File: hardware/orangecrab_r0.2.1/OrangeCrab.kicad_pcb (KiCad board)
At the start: 6 copper layers, 50.8 x 22.9 mm, 163 parts, among them J1 Conn_01x12_Male, J2 Conn_01x16_Male, J3 USB_C_Receptacle_USB2.0, J4 MicroSd, J5 JST, J6 Conn_01x05_Male, SW1 SW_Push, U1 TLV62569DRL, U10 NCP115-2.5, U2 TLV62569DRL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

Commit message: Added revision suffix gc1 to indicate the changed layout: 0.2.1-gc1
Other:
- board text added: "r0.2.1-gc1"
- board text removed: "r0.2.1"
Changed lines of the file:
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@@
 		(title "Orange Crab")
 		(date "2020-07-18")
-		(rev "r0.2.1")
+		(rev "r0.2.1-gc1")
 		(company "Good Stuff Department")
 		(comment 1 "ECP5 in Feather format with DDR3 x16 memory")
@@
 		)
 	)
-	(gr_text "r0.2.1"
+	(gr_text "r0.2.1-gc1"
 		(at 172.57 101.04 0)
 		(layer "B.SilkS")

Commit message: 0.2.1-gc2: Centered castelated holes to edges and reduced diameter from 1 to 0.8 mm
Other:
- board text added: "r0.2.1-gc2"
- board text removed: "r0.2.1-gc1"
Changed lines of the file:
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@@
 	(title_block
 		(title "Orange Crab")
-		(date "2020-07-18")
-		(rev "r0.2.1-gc1")
+		(date "2026-01-30")
+		(rev "r0.2.1-gc2")
 		(company "Good Stuff Department")
 		(comment 1 "ECP5 in Feather format with DDR3 x16 memory")
 		(comment 3 "Licensed under CERN OHL v.1.2")
-		(comment 4 "Designed By: Gregory Davill")
+		(comment 4 "Originally Designed By: Gregory Davill")
 	)
 	(layers
@@
 		)
 		(pad "1" thru_hole roundrect
-			(at -13.97 -1.4)
+			(at -13.97 -1.27)
 			(size 2 2)
-			(drill 1)
+			(drill 0.8)
 			(layers "*.Cu" "*.Mask")
 			(remove_unused_layers no)
@@
 		)
 		(pad "2" thru_hole circle
-			(at -11.43 -1.4)
+			(at -11.43 -1.27)
 			(size 2 2)
-			(drill 1)
+			(drill 0.8)
 			(layers "*.Cu" "*.Mask")
 			(remove_unused_layers no)
@@
 		)
 		(pad "3" thru_hole circle
-			(at -8.89 -1.4)
+			(at -8.89 -1.27)
 			(size 2 2)
-			(drill 1)
+			(drill 0.8)
 			(layers "*.Cu" "*.Mask")
 			(remove_unused_layers no)
@@
 		)
 		(pad "4" thru_hole circle
-			(at -6.35 -1.4)
+			(at -6.35 -1.27)
 			(size 2 2)
-			(drill 1)
+			(drill 0.8)
 			(layers "*.Cu" "*.Mask")
 			(remove_unused_layers no)
@@
 		)
 		(pad "5" thru_hole circle
-			(at -3.81 -1.4)
+			(at -3.81 -1.27)
 			(size 2 2)
-			(drill 1)
+			(drill 0.8)
 			(layers "*.Cu" "*.Mask")
 			(remove_unused_layers no)
@@
 		)
 		(pad "6" thru_hole circle
-			(at -1.27 -1.4)
+			(at -1.27 -1.27)
 			(size 2 2)
-			(drill 1)
+			(drill 0.8)
 			(layers "*.Cu" "*.Mask")
 			(remove_unused_layers no)
@@
 		)
 		(pad "7" thru_hole circle
-			(at 1.27 -1.4)
+			(at 1.27 -1.27)
 			(size 2 2)
-			(drill 1)
+			(drill 0.8)
 			(layers "*.Cu" "*.Mask")
 			(remove_unused_layers no)
@@
 		)
 		(pad "8" thru_hole circle
-			(at 3.81 -1.4)
+			(at 3.81 -1.27)
 			(size 2 2)
-			(drill 1)
+			(drill 0.8)
 			(layers "*.Cu" "*.Mask")
 			(remove_unused_layers no)
@@
 		)
 		(pad "9" thru_hole circle
-			(at 6.35 -1.4)
+			(at 6.35 -1.27)
 			(size 2 2)
-			(drill 1)
+			(drill 0.8)
 			(layers "*.Cu" "*.Mask")
 			(remove_unused_layers no)
@@
 		)
 		(pad "10" thru_hole circle
-			(at 8.89 -1.4)
+			(at 8.89 -1.27)
 			(size 2 2)
-			(drill 1)
+			(drill 0.8)
 			(layers "*.Cu" "*.Mask")
 			(remove_unused_layers no)
@@
 		)
 		(pad "11" thru_hole circle
-			(at 11.43 -1.4)
+			(at 11.43 -1.27)
 			(size 2 2)
-			(drill 1)
+			(drill 0.8)
 			(layers "*.Cu" "*.Mask")
 			(remove_unused_layers no)
@@
 		)
 		(pad "12" thru_hole circle
-			(at 13.97 -1.4)
+			(at 13.97 -1.27)
 			(size 2 2)
-			(drill 1)
+			(drill 0.8)
 			(layers "*.Cu" "*.Mask")
 			(remove_unused_layers no)
@@
 		)
 		(pad "1" thru_hole roundrect
-			(at -19.05 1.4)
+			(at -19.05 1.27)
 			(size 2 2)
-			(drill 1)
+			(drill 0.8)
 			(layers "*.Cu" "*.Mask")
 			(remove_unused_layers no)
@@
 		)
 		(pad "2" thru_hole circle
-			(at -16.51 1.4)
+			(at -16.51 1.27)
 			(size 2 2)
-			(drill 1)
+			(drill 0.8)
 			(layers "*.Cu" "*.Mask")
 			(remove_unused_layers no)
@@
 		)
 		(pad "3" thru_hole circle
-			(at -13.97 1.4)
+			(at -13.97 1.27)
 			(size 2 2)
-			(drill 1)
+			(drill 0.8)
 			(layers "*.Cu" "*.Mask")
 			(remove_unused_layers no)
@@
 		)
 		(pad "4" thru_hole circle
-			(at -11.43 1.4)
+			(at -11.43 1.27)
 			(size 2 2)
-			(drill 1)
+			(drill 0.8)
 			(layers "*.Cu" "*.Mask")
 			(remove_unused_layers no)
@@
 		)
 		(pad "5" thru_hole circle
-			(at -8.89 1.4)
+			(at -8.89 1.27)
 			(size 2 2)
-			(drill 1)
+			(drill 0.8)
 			(layers "*.Cu" "*.Mask")
 			(remove_unused_layers no)
@@
 		)
 		(pad "6" thru_hole circle
-			(at -6.35 1.4)
+			(at -6.35 1.27)
 			(size 2 2)
-			(drill 1)
+			(drill 0.8)
 			(layers "*.Cu" "*.Mask")
 			(remove_unused_layers no)
@@
 		)
 		(pad "7" thru_hole circle
-			(at -3.81 1.4)
+			(at -3.81 1.27)
 			(size 2 2)
-			(drill 1)
+			(drill 0.8)
 			(layers "*.Cu" "*.Mask")
 			(remove_unused_layers no)
@@
 		)
 		(pad "8" thru_hole circle
-			(at -1.27 1.4)
+			(at -1.27 1.27)
 			(size 2 2)
-			(drill 1)
+			(drill 0.8)
 			(layers "*.Cu" "*.Mask")
 			(remove_unused_layers no)
@@
 		)
 		(pad "9" thru_hole circle
-			(at 1.27 1.4)
+			(at 1.27 1.27)
 			(size 2 2)
-			(drill 1)
+			(drill 0.8)
 			(layers "*.Cu" "*.Mask")
 			(remove_unused_layers no)
@@
 		)
 		(pad "10" thru_hole circle
-			(at 3.81 1.4)
+			(at 3.81 1.27)
 			(size 2 2)
-			(drill 1)
+			(drill 0.8)
 			(layers "*.Cu" "*.Mask")
 			(remove_unused_layers no)
@@
 		)
 		(pad "11" thru_hole circle
-			(at 6.35 1.4)
+			(at 6.35 1.27)
 			(size 2 2)
-			(drill 1)
+			(drill 0.8)
 			(layers "*.Cu" "*.Mask")
 			(remove_unused_layers no)
@@
 		)
 		(pad "12" thru_hole circle
-			(at 8.89 1.4)
+			(at 8.89 1.27)
 			(size 2 2)
-			(drill 1)
+			(drill 0.8)
 			(layers "*.Cu" "*.Mask")
 			(remove_unused_layers no)
@@
 		)
 		(pad "13" thru_hole circle
-			(at 11.43 1.4)
+			(at 11.43 1.27)
 			(size 2 2)
-			(drill 1)
+			(drill 0.8)
 			(layers "*.Cu" "*.Mask")
 			(remove_unused_layers no)
@@
 		)
 		(pad "14" thru_hole circle
-			(at 13.97 1.4)
+			(at 13.97 1.27)
 			(size 2 2)
-			(drill 1)
+			(drill 0.8)
 			(layers "*.Cu" "*.Mask")
 			(remove_unused_layers no)
@@
 		)
 		(pad "15" thru_hole circle
-			(at 16.51 1.4)
+			(at 16.51 1.27)
 			(size 2 2)
-			(drill 1)
+			(drill 0.8)
 			(layers "*.Cu" "*.Mask")
 			(remove_unused_layers no)
@@
 		)
 		(pad "16" thru_hole circle
-			(at 19.05 1.4)
+			(at 19.05 1.27)
 			(size 2 2)
-			(drill 1)
+			(drill 0.8)
 			(layers "*.Cu" "*.Mask")
 			(remove_unused_layers no)
@@
 		)
 	)
-	(gr_text "r0.2.1-gc1"
+	(gr_text "r0.2.1-gc2"
 		(at 172.57 101.04 0)
 		(layer "B.SilkS")

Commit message: 0.2.1-li1: Changed the type pads of castellated holes in KiCAD to flag they are castellated holes. Moved version string for better visibility. Added missing USB connector to BOM. Changed from 25F to 85F variant.
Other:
- board text added: "2026-04-22"
- board text added: "r0.2.1-li1"
- board text removed: "2020-07-18"
- board text removed: "r0.2.1-gc2"
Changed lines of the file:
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@@
 		(title "Orange Crab")
 		(date "2026-01-30")
-		(rev "r0.2.1-gc2")
+		(rev "r0.2.1-li1")
 		(company "Good Stuff Department")
 		(comment 1 "ECP5 in Feather format with DDR3 x16 memory")
@@
 			(drillshape 0)
 			(scaleselection 1)
-			(outputdirectory "output/")
+			(outputdirectory "2026-04-22-li1")
 		)
 	)
@@
 			(size 2 2)
 			(drill 0.8)
+			(property pad_prop_castellated)
 			(layers "*.Cu" "*.Mask")
 			(remove_unused_layers no)
@@
 			(size 2 2)
 			(drill 0.8)
+			(property pad_prop_castellated)
 			(layers "*.Cu" "*.Mask")
 			(remove_unused_layers no)
@@
 			(size 2 2)
 			(drill 0.8)
+			(property pad_prop_castellated)
 			(layers "*.Cu" "*.Mask")
 			(remove_unused_layers no)
@@
 			(size 2 2)
 			(drill 0.8)
+			(property pad_prop_castellated)
 			(layers "*.Cu" "*.Mask")
 			(remove_unused_layers no)
@@
 			(size 2 2)
 			(drill 0.8)
+			(property pad_prop_castellated)
 			(layers "*.Cu" "*.Mask")
 			(remove_unused_layers no)
@@
 			(size 2 2)
 			(drill 0.8)
+			(property pad_prop_castellated)
 			(layers "*.Cu" "*.Mask")
 			(remove_unused_layers no)
@@
 			(size 2 2)
 			(drill 0.8)
+			(property pad_prop_castellated)
 			(layers "*.Cu" "*.Mask")
 			(remove_unused_layers no)
@@
 			(size 2 2)
 			(drill 0.8)
+			(property pad_prop_castellated)
 			(layers "*.Cu" "*.Mask")
 			(remove_unused_layers no)
@@
 			(size 2 2)
 			(drill 0.8)
+			(property pad_prop_castellated)
 			(layers "*.Cu" "*.Mask")
 			(remove_unused_layers no)
@@
 			(size 2 2)
 			(drill 0.8)
+			(property pad_prop_castellated)
 			(layers "*.Cu" "*.Mask")
 			(remove_unused_layers no)
@@
 			(size 2 2)
 			(drill 0.8)
+			(property pad_prop_castellated)
 			(layers "*.Cu" "*.Mask")
 			(remove_unused_layers no)
@@
 			(size 2 2)
 			(drill 0.8)
+			(property pad_prop_castellated)
 			(layers "*.Cu" "*.Mask")
 			(remove_unused_layers no)
@@
 			(size 2 2)
 			(drill 0.8)
+			(property pad_prop_castellated)
 			(layers "*.Cu" "*.Mask")
 			(remove_unused_layers no)
@@
 			(net 61 "P3.3V")
 		)
-		(pad "2" thru_hole circle
-			(at -16.51 1.27)
-			(size 2 2)
-			(drill 0.8)
-			(layers "*.Cu" "*.Mask")
-			(remove_unused_layers no)
-			(net 61 "P3.3V")
-		)
 		(pad "3" thru_hole circle
 			(at -13.97 0)
@@
 			(size 2 2)
 			(drill 0.8)
+			(property pad_prop_castellated)
 			(layers "*.Cu" "*.Mask")
 			(remove_unused_layers no)
@@
 			(size 2 2)
 			(drill 0.8)
+			(property pad_prop_castellated)
 			(layers "*.Cu" "*.Mask")
 			(remove_unused_layers no)
@@
 			(size 2 2)
 			(drill 0.8)
+			(property pad_prop_castellated)
 			(layers "*.Cu" "*.Mask")
 			(remove_unused_layers no)
@@
 			(size 2 2)
 			(drill 0.8)
+			(property pad_prop_castellated)
 			(layers "*.Cu" "*.Mask")
 			(remove_unused_layers no)
@@
 			(size 2 2)
 			(drill 0.8)
+			(property pad_prop_castellated)
 			(layers "*.Cu" "*.Mask")
 			(remove_unused_layers no)
@@
 			(size 2 2)
 			(drill 0.8)
+			(property pad_prop_castellated)
 			(layers "*.Cu" "*.Mask")
 			(remove_unused_layers no)
@@
 			(size 2 2)
 			(drill 0.8)
+			(property pad_prop_castellated)
 			(layers "*.Cu" "*.Mask")
 			(remove_unused_layers no)
@@
 			(size 2 2)
 			(drill 0.8)
+			(property pad_prop_castellated)
 			(layers "*.Cu" "*.Mask")
 			(remove_unused_layers no)
@@
 			(size 2 2)
 			(drill 0.8)
+			(property pad_prop_castellated)
 			(layers "*.Cu" "*.Mask")
 			(remove_unused_layers no)
@@
 			(size 2 2)
 			(drill 0.8)
+			(property pad_prop_castellated)
 			(layers "*.Cu" "*.Mask")
 			(remove_unused_layers no)
@@
 			(size 2 2)
 			(drill 0.8)
+			(property pad_prop_castellated)
 			(layers "*.Cu" "*.Mask")
 			(remove_unused_layers no)
@@
 			(size 2 2)
 			(drill 0.8)
+			(property pad_prop_castellated)
 			(layers "*.Cu" "*.Mask")
 			(remove_unused_layers no)
@@
 			(size 2 2)
 			(drill 0.8)
+			(property pad_prop_castellated)
 			(layers "*.Cu" "*.Mask")
 			(remove_unused_layers no)
@@
 			(size 2 2)
 			(drill 0.8)
+			(property pad_prop_castellated)
 			(layers "*.Cu" "*.Mask")
 			(remove_unused_layers no)
 			(net 1 "GND")
 		)
+		(pad "e" thru_hole circle
+			(at -16.51 1.27)
+			(size 2 2)
+			(drill 0.8)
+			(property pad_prop_castellated)
+			(layers "*.Cu" "*.Mask")
+			(remove_unused_layers no)
+			(net 61 "P3.3V")
+		)
 		(embedded_fonts no)
 	)
@@
 		(layer "Edge.Cuts")
 	)
-	(gr_text "2020-07-18\n"
+	(gr_text "2026-04-22\n"
 		(at 184.26 98.525 90)
 		(layer "B.Cu")
@@
 		)
 	)
-	(gr_text "r0.2.1-gc2"
-		(at 172.57 101.04 0)
+	(gr_text "r0.2.1-li1"
+		(at 183 99 90)
 		(layer "B.SilkS")
 		(effects
@@
 				(thickness 0.2)
 			)
-			(justify mirror)
+			(justify left mirror)
 		)
 	)

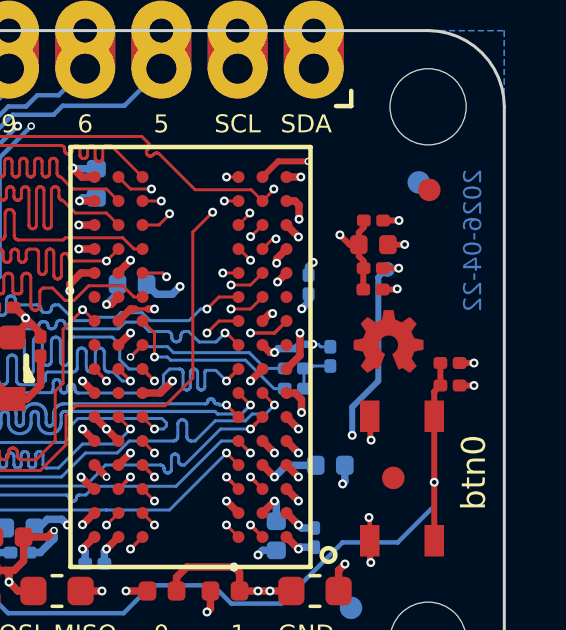
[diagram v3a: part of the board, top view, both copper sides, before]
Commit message: 0.2.1-lsi2: Added 1 mm 'produced by' mark
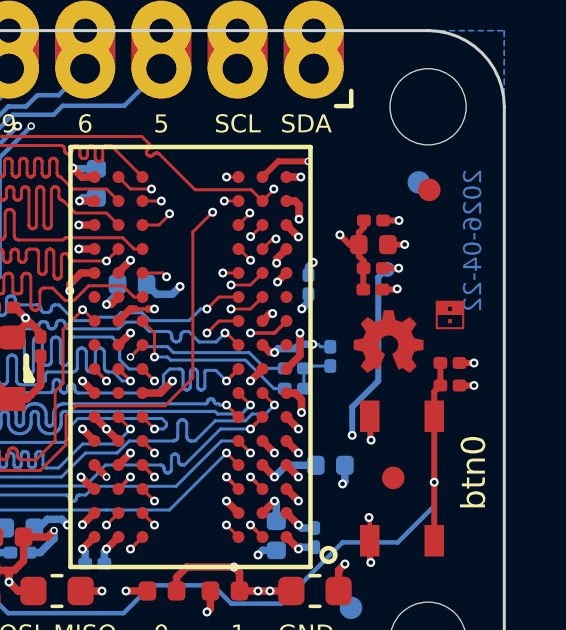
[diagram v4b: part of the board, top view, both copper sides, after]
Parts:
- added lsi-logo: G***, logo:lsi-logo-no-text-1mm, F.Cu at (183.5, 101.0)
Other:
- board text added: "r0.2.1-lsi2"
- board text removed: "r0.2.1-li1"
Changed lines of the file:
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@@
 	(title_block
 		(title "Orange Crab")
-		(date "2026-01-30")
-		(rev "r0.2.1-li1")
+		(date "2026-05-31")
+		(rev "r0.2.1-lsi2")
 		(company "Good Stuff Department")
 		(comment 1 "ECP5 in Feather format with DDR3 x16 memory")
@@
 		(embedded_fonts no)
 	)
+	(footprint "logo:lsi-logo-no-text-1mm"
+		(layer "F.Cu")
+		(at 183.5 101)
+		(descr "Converted using: svg2mod -i lsi/code/media/logo-no-text-kicad-mask.svg --units mm -f 0.1345 -c -o lsi-logo-no-text-1mm")
+		(tags "svg2mod")
+		(property "Reference" "lsi-logo"
+			(at 0 -3.552072 0)
+			(layer "F.SilkS")
+			(hide yes)
+			(effects
+				(font
+					(size 1.524 1.524)
+					(thickness 0.3048)
+				)
+			)
+		)
+		(property "Value" "G***"
+			(at 0 3.552072 0)
+			(layer "F.SilkS")
+			(hide yes)
+			(effects
+				(font
+					(size 1.524 1.524)
+					(thickness 0.3048)
+				)
+			)
+		)
+		(property "Datasheet" ""
+			(at 0 0 0)
+			(layer "F.Fab")
+			(hide yes)
+			(effects
+				(font
+					(size 1.27 1.27)
+					(thickness 0.15)
+				)
+			)
+		)
+		(property "Description" ""
+			(at 0 0 0)
+			(layer "F.Fab")
+			(hide yes)
+			(effects
+				(font
+					(size 1.27 1.27)
+					(thickness 0.15)
+				)
+			)
+		)
+		(attr exclude_from_pos_files exclude_from_bom)
+		(fp_poly
+			(pts
+				(xy 0.067862 0.271429) (xy 0.067862 0.135718) (xy -0.06785 0.135718) (xy -0.06785 0.271429) (xy 0.067862 0.271429)
+			)
+			(stroke
+				(width 0)
+				(type solid)
+			)
+			(fill yes)
+			(layer "F.Cu")
+		)
+		(fp_poly
+			(pts
+				(xy 0.474997 0.474997) (xy 0.474997 -0.474997) (xy -0.474997 -0.474997) (xy -0.474997 0.474997)
+				(xy 0.40714 0.474997) (xy 0.40714 0.40714) (xy -0.40714 0.40714) (xy -0.40714 0) (xy 0.067857 0)
+				(xy 0.067857 -0.135713) (xy -0.067857 -0.135713) (xy -0.067857 -0.271427) (xy 0.067857 -0.271427)
+				(xy 0.067857 -0.135713) (xy 0.067857 0) (xy 0.40714 0) (xy 0.40714 0.40714) (xy 0.40714 0.474997)
+				(xy 0.474997 0.474997)
+			)
+			(stroke
+				(width 0)
+				(type solid)
+			)
+			(fill yes)
+			(layer "F.Cu")
+		)
+		(fp_poly
+			(pts
+				(xy -0.504072 -0.504072) (xy -0.504072 0.504072) (xy 0.504072 0.504072) (xy 0.504072 -0.504072)
+				(xy -0.504072 -0.504072)
+			)
+			(stroke
+				(width 0)
+				(type solid)
+			)
+			(fill yes)
+			(layer "F.Mask")
+		)
+		(embedded_fonts no)
+	)
 	(footprint "Resistor_SMD:R_0402_1005Metric"
 		(layer "B.Cu")
@@
 		)
 	)
-	(gr_text "r0.2.1-li1"
+	(gr_text "r0.2.1-lsi2"
 		(at 183 99 90)
 		(layer "B.SilkS")
